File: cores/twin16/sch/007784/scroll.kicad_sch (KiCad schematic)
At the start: 90 parts, among them J1 A4H, J53 FDN, J60 R8B, J66 N8B, J75 N2B, J78 N2P, J81 R2N, K1 A4H, K71 FDO, K80 R2P, M1 FDN, M15 FDN, M22 FDN, M29 FDN, M36 FDN, M43 FDN, M50 FDN, M57 FDN, M64 FDN, M71 FDN, M8 FDN, P1 A4H, P51 R8B, P57 FDN, P64 FDN, P71 FDN, P78 N2P, Q1 FDO, Q15 FDO, Q22 FDO, Q29 FDN, Q36 FDO, Q50 FDO, Q57 N2B, Q8 FDN

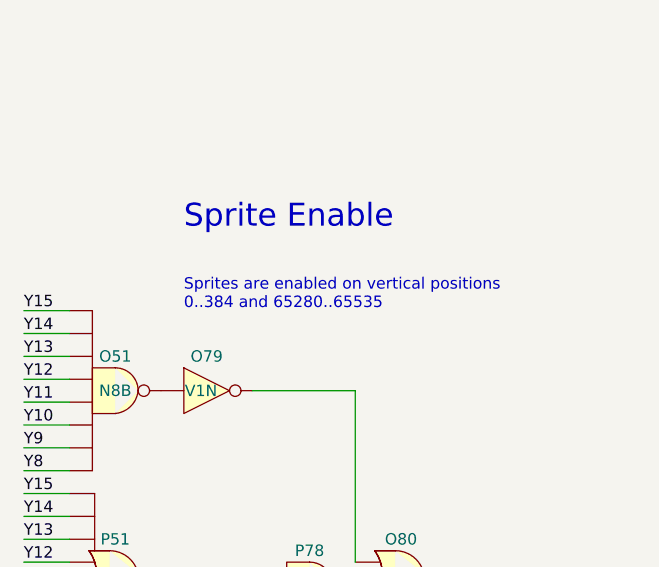
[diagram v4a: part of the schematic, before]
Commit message: twin16: boots up to RAM/ROM check screen
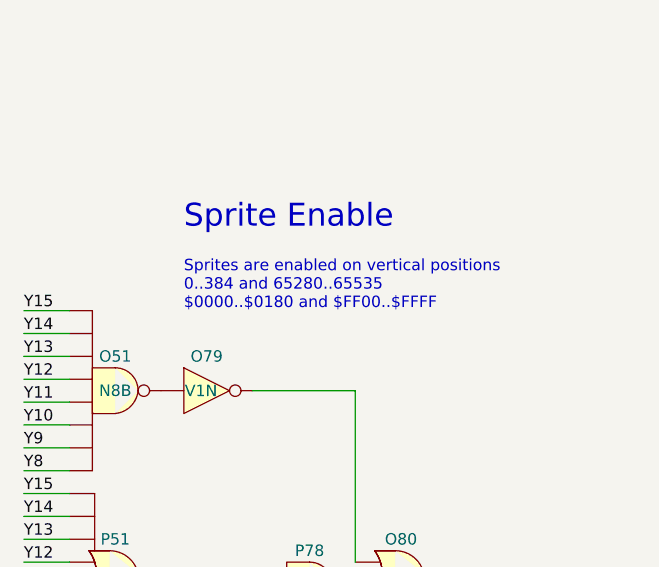
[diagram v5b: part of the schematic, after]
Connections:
- net at J78.: now also J75.; no longer J60.
- net at O80.: now also L78.; no longer O79.
- net at P78.: now also Q57.; no longer O80.
- net at K80.: now also J81.; no longer J78.
- net at J81.: now also H79.; no longer K80.
- new net: F19. (~{R}), F28. (~{R}), F60. (~{R}), F70. (~{R}), F78. (~{R}), F86. (~{R}), G71. (~{R}), G82. (~{R}), R63.
- new net: E28. (S4), F70. (~{R})
- new net: A71. (~{R}), E78. (~{R}), E86. (~{R}), F52. (~{R}), H41. (~{R}), H48. (~{R}), I71. (~{R}), I86. (~{R}), R59.
- new net: I21. (S4), I71. (~{R})
- new net: O57. (~{R}), O64. (~{R}), O73. (~{R}), Q1. (~{R}), Q15. (~{R}), Q22. (~{R}), Q36. (~{R}), Q50. (~{R}), R17.
- new net: P1. (S4), Q36. (~{R})
- new net: J60., J78.
- new net: F19. (~{R}), G21. (S4)
- new net: E28. (S4), G21. (S4)
- new net: G21. (S4), G82. (~{R})
- new net: F60. (~{R}), G21. (S4)
- new net: G21. (S4), G71. (~{R})
- new net: G21. (S4), J1. (S4)
- new net: E28. (S4), F78. (~{R})
- new net: O1. (S4), O57. (~{R})
- new net: O79., O80.
- new net: O80., P78.
- new net: K71. (~{R}), L29. (~{R}), L36. (~{R}), L43. (~{R}), L50. (~{R}), L57. (~{R}), L64. (~{R}), L71. (~{R}), R21.
- new net: J1. (S4), L50. (~{R})
- new net: J1. (S4), L43. (~{R})
- new net: A71. (~{R}), D28. (S4)
- new net: J78., K80.
- new net: H41. (~{R}), I21. (S4)
- new net: K1. (S4), L64. (~{R})
- new net: P1. (S4), Q50. (~{R})
- new net: K1. (S4), L57. (~{R})
- new net: D28. (S4), E86. (~{R})
- new net: P51., P78.
- new net: K80., L78.
- new net: E28. (S4), F28. (~{R})
- new net: K1. (S4), L71. (~{R})
- new net: D28. (S4), F52. (~{R})
- new net: J66., J81.
- new net: E28. (S4), F86. (~{R})
- new net: P1. (S4), Q15. (~{R})
- new net: P1. (S4), Q1. (~{R})
- new net: J1. (S4), K71. (~{R})
- new net: O1. (S4), O64. (~{R})
- new net: K1. (S4), L29. (~{R})
- new net: I21. (S4), P1. (S4)
- new net: O1. (S4), P1. (S4)
- new net: I21. (S4), I86. (~{R})
- new net: D28. (S4), E78. (~{R})
- new net: O1. (S4), Q22. (~{R})
- new net: D28. (S4), I21. (S4)
- new net: O1. (S4), O73. (~{R})
- new net: J1. (S4), L36. (~{R})
- new net: H48. (~{R}), I21. (S4)
- new net: J1. (S4), K1. (S4)
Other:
- note added: "Sprites are enabled on vertical positions 0..384 and 65280..65535 $0000..$0180 and $FF00..$FFFF"
- note removed: "Sprites are enabled on vertical positions 0..384 and 65280..65535"
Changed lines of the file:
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@@
 		)
 	)
-	(text "Sprites are enabled on vertical positions\n0..384 and 65280..65535"
+	(text "Sprites are enabled on vertical positions\n0..384 and 65280..65535\n$0000..$0180 and $FF00..$FFFF"
 		(exclude_from_sim no)
 		(at 341.63 95.25 0)

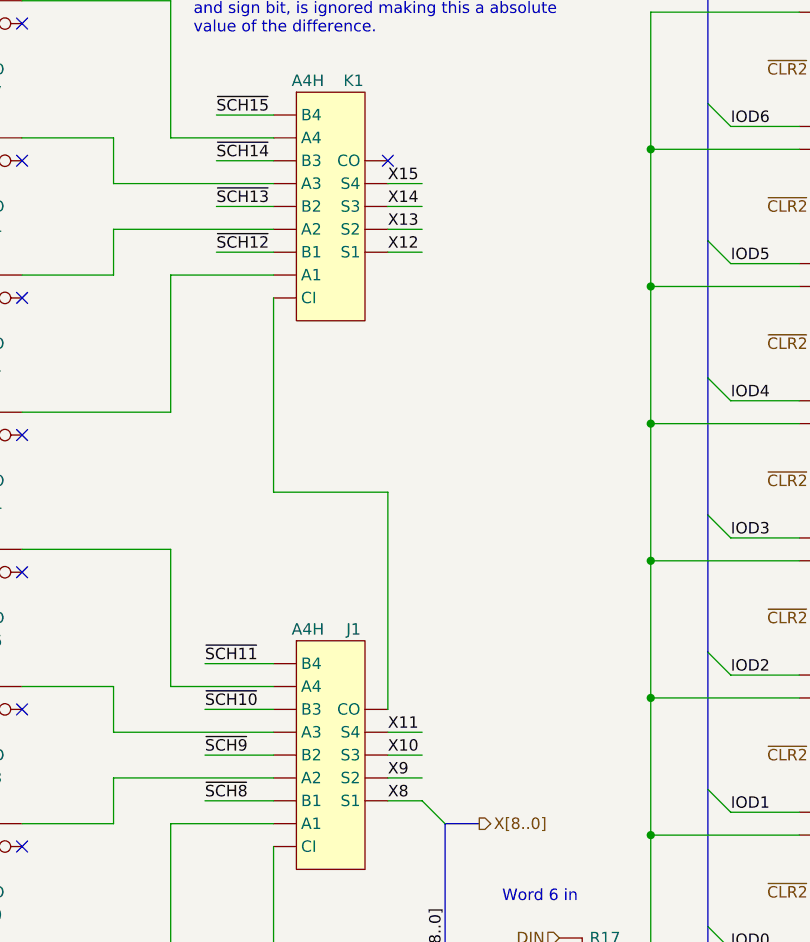
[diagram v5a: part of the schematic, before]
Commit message: twin16/fround: better implementation of K00788x chipset
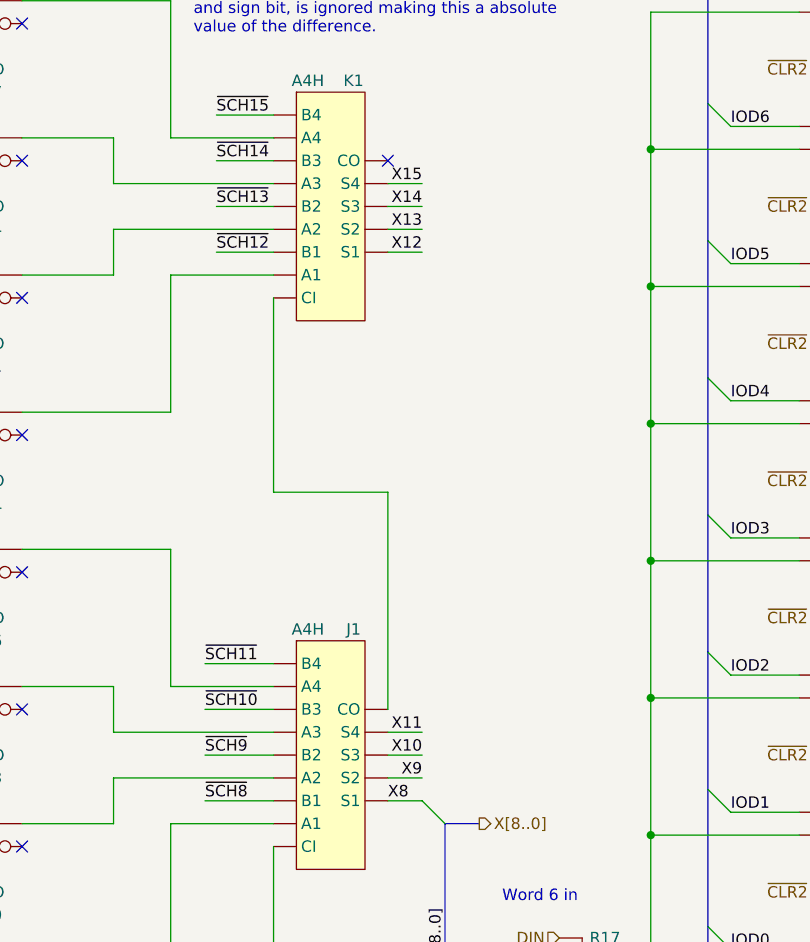
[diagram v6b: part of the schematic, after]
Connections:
- net at J78.: now also J75.; no longer J60.
- net at O80.: now also L78.; no longer O79.
- net at P78.: now also Q57.; no longer O80.
- net at K80.: now also J81.; no longer J78.
- net at J81.: now also H79.; no longer K80.
- new net: F19. (~{R}), F28. (~{R}), F60. (~{R}), F70. (~{R}), F78. (~{R}), F86. (~{R}), G71. (~{R}), G82. (~{R}), R63.
- new net: E28. (S4), F70. (~{R})
- new net: A71. (~{R}), E78. (~{R}), E86. (~{R}), F52. (~{R}), H41. (~{R}), H48. (~{R}), I71. (~{R}), I86. (~{R}), R59.
- new net: I21. (S4), I71. (~{R})
- new net: O57. (~{R}), O64. (~{R}), O73. (~{R}), Q1. (~{R}), Q15. (~{R}), Q22. (~{R}), Q36. (~{R}), Q50. (~{R}), R17.
- new net: P1. (S4), Q36. (~{R})
- new net: J60., J78.
- new net: F19. (~{R}), G21. (S4)
- new net: E28. (S4), G21. (S4)
- new net: G21. (S4), G82. (~{R})
- new net: F60. (~{R}), G21. (S4)
- new net: G21. (S4), G71. (~{R})
- new net: G21. (S4), J1. (S4)
- new net: E28. (S4), F78. (~{R})
- new net: O1. (S4), O57. (~{R})
- new net: O79., O80.
- new net: O80., P78.
- new net: K71. (~{R}), L29. (~{R}), L36. (~{R}), L43. (~{R}), L50. (~{R}), L57. (~{R}), L64. (~{R}), L71. (~{R}), R21.
- new net: J1. (S4), L50. (~{R})
- new net: J1. (S4), L43. (~{R})
- new net: A71. (~{R}), D28. (S4)
- new net: J78., K80.
- new net: H41. (~{R}), I21. (S4)
- new net: K1. (S4), L64. (~{R})
- new net: P1. (S4), Q50. (~{R})
- new net: K1. (S4), L57. (~{R})
- new net: D28. (S4), E86. (~{R})
- new net: P51., P78.
- new net: K80., L78.
- new net: E28. (S4), F28. (~{R})
- new net: K1. (S4), L71. (~{R})
- new net: D28. (S4), F52. (~{R})
- new net: J66., J81.
- new net: E28. (S4), F86. (~{R})
- new net: P1. (S4), Q15. (~{R})
- new net: P1. (S4), Q1. (~{R})
- new net: J1. (S4), K71. (~{R})
- new net: O1. (S4), O64. (~{R})
- new net: K1. (S4), L29. (~{R})
- new net: I21. (S4), P1. (S4)
- new net: O1. (S4), P1. (S4)
- new net: I21. (S4), I86. (~{R})
- new net: D28. (S4), E78. (~{R})
- new net: O1. (S4), Q22. (~{R})
- new net: D28. (S4), I21. (S4)
- new net: O1. (S4), O73. (~{R})
- new net: J1. (S4), L36. (~{R})
- new net: H48. (~{R}), I21. (S4)
- new net: J1. (S4), K1. (S4)
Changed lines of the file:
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@@
 	)
 	(label "X14"
-		(at 189.23 59.69 0)
-		(fields_autoplaced yes)
-		(effects
-			(font
-				(size 1.27 1.27)
-			)
-			(justify left bottom)
+		(at 193.04 59.69 180)
+		(fields_autoplaced yes)
+		(effects
+			(font
+				(size 1.27 1.27)
+			)
+			(justify right bottom)
 		)
 	)
 	(label "X15"
-		(at 189.23 57.15 0)
-		(fields_autoplaced yes)
-		(effects
-			(font
-				(size 1.27 1.27)
-			)
-			(justify left bottom)
+		(at 193.04 57.15 180)
+		(fields_autoplaced yes)
+		(effects
+			(font
+				(size 1.27 1.27)
+			)
+			(justify right bottom)
 		)
 	)
@@
 	)
 	(label "X10"
-		(at 189.23 120.65 0)
-		(fields_autoplaced yes)
-		(effects
-			(font
-				(size 1.27 1.27)
-			)
-			(justify left bottom)
+		(at 193.04 120.65 180)
+		(fields_autoplaced yes)
+		(effects
+			(font
+				(size 1.27 1.27)
+			)
+			(justify right bottom)
 		)
 	)
@@
 	)
 	(label "X12"
-		(at 189.23 64.77 0)
-		(fields_autoplaced yes)
-		(effects
-			(font
-				(size 1.27 1.27)
-			)
-			(justify left bottom)
+		(at 193.04 64.77 180)
+		(fields_autoplaced yes)
+		(effects
+			(font
+				(size 1.27 1.27)
+			)
+			(justify right bottom)
 		)
 	)
@@
 	)
 	(label "X9"
-		(at 189.23 123.19 0)
-		(fields_autoplaced yes)
-		(effects
-			(font
-				(size 1.27 1.27)
-			)
-			(justify left bottom)
+		(at 193.04 123.19 180)
+		(fields_autoplaced yes)
+		(effects
+			(font
+				(size 1.27 1.27)
+			)
+			(justify right bottom)
 		)
 	)
@@
 	)
 	(label "X13"
-		(at 189.23 62.23 0)
-		(fields_autoplaced yes)
-		(effects
-			(font
-				(size 1.27 1.27)
-			)
-			(justify left bottom)
+		(at 193.04 62.23 180)
+		(fields_autoplaced yes)
+		(effects
+			(font
+				(size 1.27 1.27)
+			)
+			(justify right bottom)
 		)
 	)
@@
 	)
 	(label "X11"
-		(at 189.23 118.11 0)
-		(fields_autoplaced yes)
-		(effects
-			(font
-				(size 1.27 1.27)
-			)
-			(justify left bottom)
-		)
-	)
+		(at 193.04 118.11 180)
+		(fields_autoplaced yes)
+		(effects
+			(font
+				(size 1.27 1.27)
+			)
+			(justify right bottom)
+		)
+	)
